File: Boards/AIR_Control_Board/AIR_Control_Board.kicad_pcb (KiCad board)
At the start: 2 copper layers, 65 x 55 mm, 79 parts, among them IC1 ATMEGA16M1, J1 MicroFit_RA_10, J2 MM_F_VT_20, J3 MicroFit_RA_V_2, J4 CONN_02X03, Q1 SSM3K333R, Q2 SSM3K333R, Q3 SSM3K333R, Q4 SSM3K333R, Q5 SSM3K333R, Q6 SSM3K333R, U1 MCP2561-E_SN, U2 TPS561201, Y1 Crystal_SMD

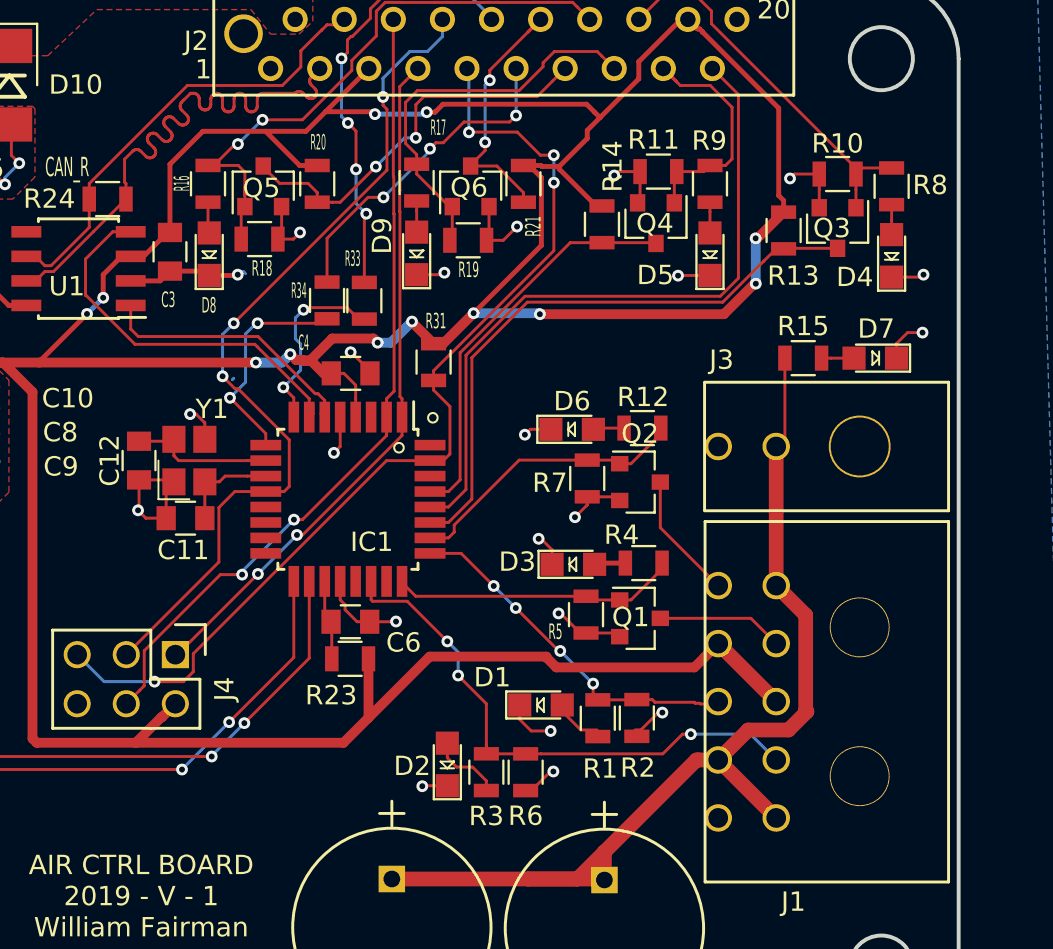
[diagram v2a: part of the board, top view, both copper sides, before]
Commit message: new gbr file with better annotations
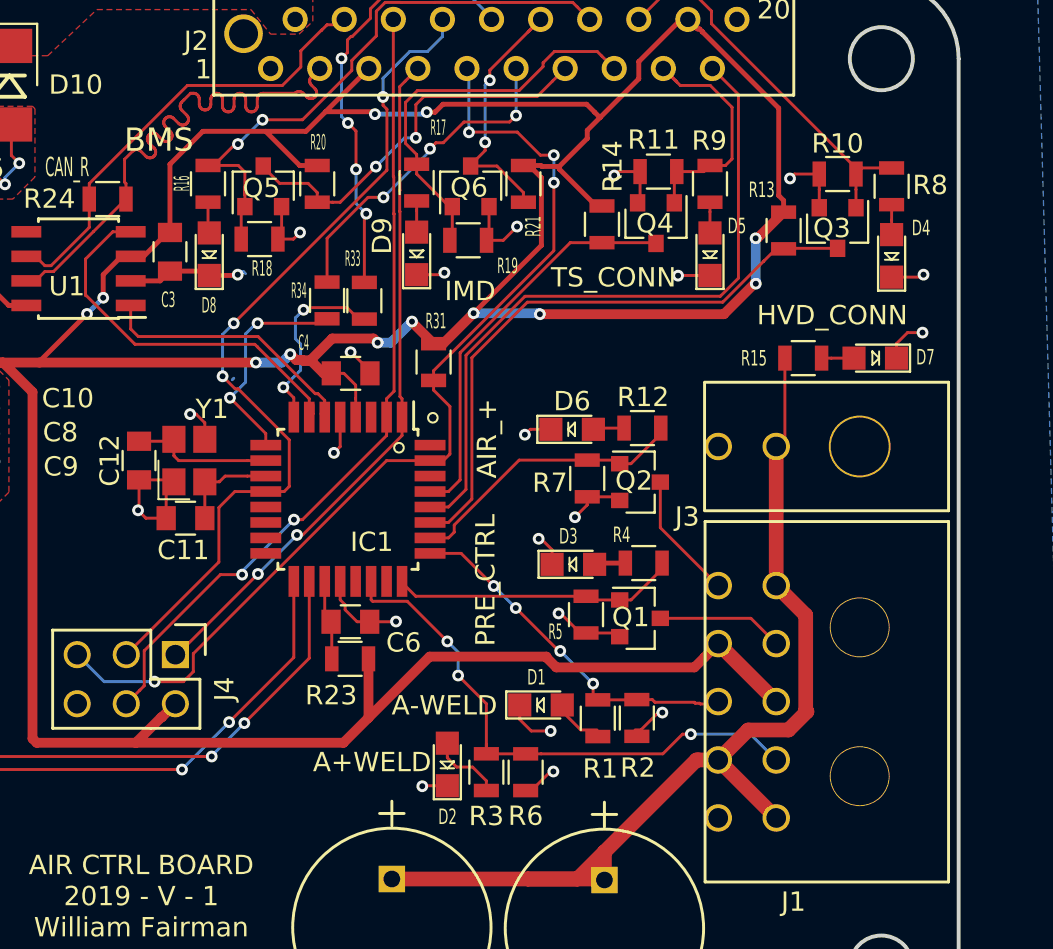
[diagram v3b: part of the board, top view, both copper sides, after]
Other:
- board text added: "A+WELD"
- board text added: "A-WELD"
- board text added: "AIR_+"
- board text added: "BMS"
- board text added: "HVD_CONN"
- board text added: "IMD"
- board text added: "PRE_CTRL"
- board text added: "TS_CONN"
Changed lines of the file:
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@@
   (general
     (thickness 1.6)
-    (drawings 30)
+    (drawings 38)
     (tracks 1023)
     (zones 0)
@@
   )
   (setup
-    (last_trace_width 0.1524)
+    (last_trace_width 0.254)
     (user_trace_width 0.1524)
     (user_trace_width 0.254)
@@
     (tags "LED led 0805 SMD smd SMT smt smdled SMDLED smtled SMTLED")
     (attr smd)
-    (fp_text reference D1 (at -2.51986 -1.42494) (layer F.SilkS)
-      (effects (font (size 1 1) (thickness 0.15)))
+    (fp_text reference D1 (at -0.23894 -1.43002) (layer F.SilkS)
+      (effects (font (size 0.8 0.5) (thickness 0.125)))
     )
     (fp_text value LED_0805 (at 0.508 2.032) (layer F.Fab) hide
@@
     (tags "resistor 0805")
     (attr smd)
-    (fp_text reference R13 (at 2.34188 -0.50292) (layer F.SilkS)
-      (effects (font (size 1 1) (thickness 0.15)))
+    (fp_text reference R13 (at -2.10312 1.13284) (layer F.SilkS)
+      (effects (font (size 0.8 0.5) (thickness 0.125)))
     )
     (fp_text value R_10K (at 0 1.75 270) (layer F.Fab) hide
@@
     (tags "resistor 0805")
     (attr smd)
-    (fp_text reference R15 (at 0 -1.651) (layer F.SilkS)
-      (effects (font (size 1 1) (thickness 0.15)))
+    (fp_text reference R15 (at -2.55016 0.01016) (layer F.SilkS)
+      (effects (font (size 0.8 0.5) (thickness 0.125)))
     )
     (fp_text value R_1K (at 0 1.75) (layer F.Fab) hide
@@
     (tags SOT-23)
     (attr smd)
-    (fp_text reference Q2 (at 0 -2.5) (layer F.SilkS)
+    (fp_text reference Q2 (at -0.31242 -0.06858) (layer F.SilkS)
       (effects (font (size 1 1) (thickness 0.15)))
     )
@@
     (tags "LED led 0805 SMD smd SMT smt smdled SMDLED smtled SMTLED")
     (attr smd)
-    (fp_text reference D3 (at -2.9005 -0.127) (layer F.SilkS)
-      (effects (font (size 1 1) (thickness 0.15)))
+    (fp_text reference D3 (at -0.26144 -1.4478) (layer F.SilkS)
+      (effects (font (size 0.8 0.5) (thickness 0.125)))
     )
     (fp_text value LED_0805 (at 0.508 2.032) (layer F.Fab) hide
@@
     (tags "resistor 0805")
     (attr smd)
-    (fp_text reference R19 (at 0.02286 1.52908) (layer F.SilkS)
+    (fp_text reference R19 (at 2.03962 1.32588) (layer F.SilkS)
       (effects (font (size 0.8 0.4) (thickness 0.1)))
     )
@@
     (tags "LED led 0805 SMD smd SMT smt smdled SMDLED smtled SMTLED")
     (attr smd)
-    (fp_text reference D5 (at -1.0844 -2.82448 180) (layer F.SilkS)
-      (effects (font (size 1 1) (thickness 0.15)))
+    (fp_text reference D5 (at 1.46068 1.39192 180) (layer F.SilkS)
+      (effects (font (size 0.8 0.5) (thickness 0.125)))
     )
     (fp_text value LED_0805 (at 0.508 2.032 90) (layer F.Fab) hide
@@
     (tags "LED led 0805 SMD smd SMT smt smdled SMDLED smtled SMTLED")
     (attr smd)
-    (fp_text reference D4 (at -1.1 -1.905 180) (layer F.SilkS)
-      (effects (font (size 1 1) (thickness 0.15)))
+    (fp_text reference D4 (at 1.44 1.524 180) (layer F.SilkS)
+      (effects (font (size 0.8 0.5) (thickness 0.125)))
     )
     (fp_text value LED_0805 (at 0.508 2.032 90) (layer F.Fab) hide
@@
     (tags "LED led 0805 SMD smd SMT smt smdled SMDLED smtled SMTLED")
     (attr smd)
-    (fp_text reference D2 (at -0.084 -1.8161) (layer F.SilkS)
-      (effects (font (size 1 1) (thickness 0.15)))
+    (fp_text reference D2 (at -2.71036 0.01016) (layer F.SilkS)
+      (effects (font (size 0.8 0.5) (thickness 0.125)))
     )
     (fp_text value LED_0805 (at 0.508 2.032 90) (layer F.Fab) hide
@@
     (attr smd)
     (fp_text reference R4 (at 1.143 1.4605 180) (layer F.SilkS)
-      (effects (font (size 1 1) (thickness 0.15)))
+      (effects (font (size 0.8 0.5) (thickness 0.125)))
     )
     (fp_text value R_200 (at 0 1.75 180) (layer F.Fab) hide
@@
   (module footprints:MicroFit_RA_V_2 (layer F.Cu)
     (at 183.896 106.934 270)
-    (fp_text reference J3 (at -4.48056 7.14756 180) (layer F.SilkS)
+    (fp_text reference J3 (at 3.6322 8.92556 180) (layer F.SilkS)
       (effects (font (size 1 1) (thickness 0.15)))
     )
@@
     (tags "LED led 0805 SMD smd SMT smt smdled SMDLED smtled SMTLED")
     (attr smd)
-    (fp_text reference D7 (at -0.04844 1.51892 180) (layer F.SilkS)
-      (effects (font (size 1 1) (thickness 0.15)))
+    (fp_text reference D7 (at -2.59352 0.04572 180) (layer F.SilkS)
+      (effects (font (size 0.8 0.5) (thickness 0.125)))
     )
     (fp_text value LED_0805 (at 0.508 2.032 180) (layer F.Fab) hide
@@
       (xy 21.61435 26.216765) (xy 21.849605 26.21762) (xy 22.074352 26.216386)) (layer B.SilkS) (width 0.01))
   )
+  (gr_text A-WELD (at 162.41268 120.33504) (layer F.SilkS)
+    (effects (font (size 1 1) (thickness 0.15)))
+  )
+  (gr_text A+WELD (at 158.66872 123.27128) (layer F.SilkS)
+    (effects (font (size 1 1) (thickness 0.15)))
+  )
+  (gr_text BMS (at 147.63496 91.07424) (layer F.SilkS)
+    (effects (font (size 1.2 1.2) (thickness 0.18)))
+  )
+  (gr_text IMD (at 163.73856 98.89744) (layer F.SilkS)
+    (effects (font (size 1 1) (thickness 0.2)))
+  )
+  (gr_text TS_CONN (at 171.16044 98.19132) (layer F.SilkS)
+    (effects (font (size 1 1) (thickness 0.15)))
+  )
+  (gr_text HVD_CONN (at 182.4736 100.14712) (layer F.SilkS)
+    (effects (font (size 1 1) (thickness 0.15)))
+  )
+  (gr_text AIR_+ (at 164.6174 106.52252 90) (layer F.SilkS)
+    (effects (font (size 1 1) (thickness 0.15)))
+  )
+  (gr_text PRE_CTRL (at 164.53612 113.84788 90) (layer F.SilkS)
+    (effects (font (size 1 1) (thickness 0.15)))
+  )
   (gr_text "AIR CTRL BOARD\n2019 - V - 1\nWilliam Fairman" (at 146.72564 130.20548) (layer F.SilkS)

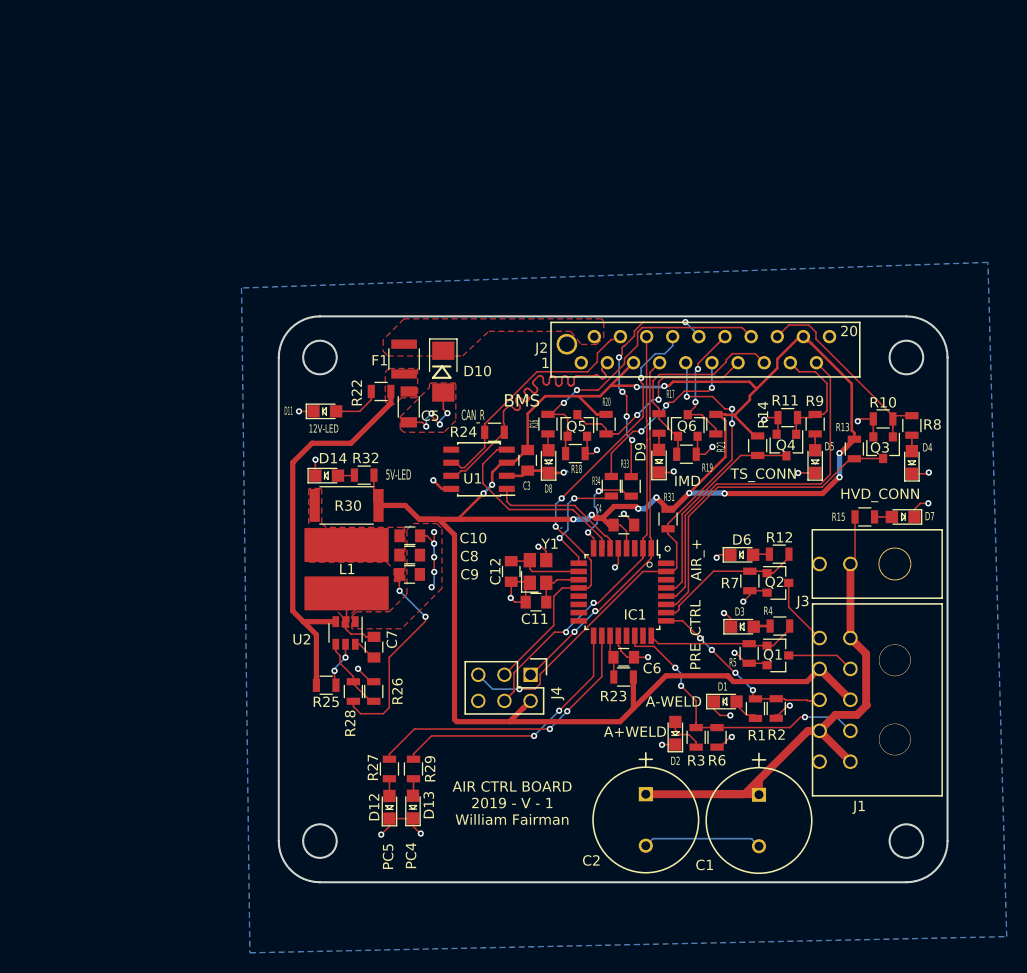
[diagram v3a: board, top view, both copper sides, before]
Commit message: updated air ctrl board and sensing board
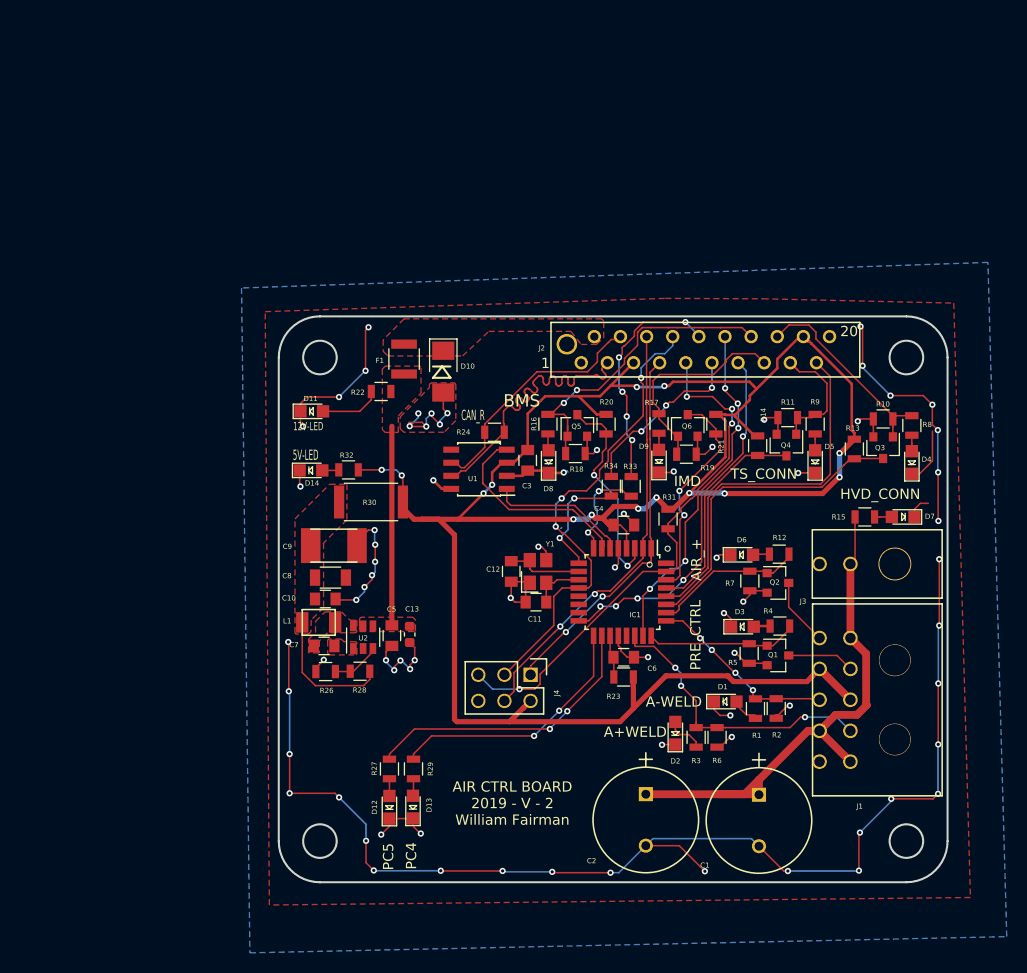
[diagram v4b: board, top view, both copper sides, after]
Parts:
- removed R25: R_10K, footprints:R_0805_OEM
- added C13: C_2.2uF, footprints:C_0603_1608Metric, F.Cu at (136.7, 113.8)
- C10: value C_0.1uF -> C_47uF
- C5: value C_22uF -> C_0.1uF; footprint footprints:C_1206_OEM -> footprints:C_0805_OEM
- C8: value C_47uF -> C_22uF; footprint footprints:C_0805_OEM -> footprints:C_1206_OEM
- C9: value C_1uF -> C_33uF; footprint footprints:C_0805_OEM -> footprints:C_1812_updated
- L1: value L_4.7uH -> L_100uH; footprint footprints:4.7uH_Inductor_OEM -> footprints:L_100uH
- R26: value R_10K -> R_25K
- R28: value R_51.1K -> R_100K
- U2: value TPS561201 -> TPS560430YF
- moved C5 22.3 mm to (135.0, 113.9)
- moved C10 10.3 mm to (128.5, 110.3)
- moved C9 10.0 mm to (127.1, 105.2)
- moved C8 8.00 mm to (129.0, 108.3)
- moved L1 5.84 mm to (127.9, 112.6), turned to 180 degrees
- moved R26 5.06 mm to (128.6, 117.4), turned to 180 degrees
- moved C7 4.85 mm to (128.4, 114.9), turned to 180 degrees
- moved R30 2.40 mm to (133.0, 100.9)
- moved R28 2.07 mm to (131.9, 117.4), turned to 180 degrees
- moved U2 1.76 mm to (132.2, 114.1), turned to 90 degrees
- moved D14 1.61 mm to (127.1, 97.8)
- moved R32 1.61 mm to (130.8, 97.8)
- moved D11 1.27 mm to (127.2, 92.1)
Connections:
- C5 pad 1: /12V_Fused -> Net-(C13-Pad1)
- F1 pad 2: /12V_Fused -> Net-(C13-Pad1)
- IC1 pad 16: Net-(IC1-Pad16) -> /BMS_Sense
- IC1 pad 23: Net-(IC1-Pad23) -> /IMD_Sense
- IC1 pad 3: Net-(IC1-Pad3) -> /ss_BMS
- IC1 pad 30: Net-(IC1-Pad30) -> /ss_IMD
- Q5 pad 3: /BMS_Sense -> /ss_BMS
- Q6 pad 3: /IMD_Sense -> /ss_IMD
- R20 pad 2: /BMS_Sense -> /ss_BMS
- R21 pad 2: /IMD_Sense -> /ss_IMD
- R22 pad 1: /12V_Fused -> Net-(C13-Pad1)
- U2 pad 1: GND -> Net-(C7-Pad1)
- U2 pad 2: Net-(C7-Pad2) -> GND
- U2 pad 3: /12V_Fused -> Net-(R26-Pad1)
- U2 pad 4: Net-(R26-Pad1) -> Net-(C13-Pad1)
- U2 pad 5: Net-(R25-Pad1) -> Net-(C13-Pad1)
- U2 pad 6: Net-(C7-Pad1) -> Net-(C7-Pad2)
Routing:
- net GND: track 101.9 -> 267.3 mm, vias 37 -> 74
- net /12V_Fused: track 38.8 -> 0.00 mm
- net /ss_IMD: track 0.00 -> 21.3 mm, vias 0 -> 2
- net /ss_BMS: track 0.00 -> 20.5 mm, vias 0 -> 2
- net /IMD_Sense: track 13.8 -> 33.9 mm, vias 2 -> 5
- net Net-(C13-Pad1): track 0.00 -> 19.3 mm
- net /BMS_Sense: track 20.6 -> 36.0 mm, vias 2 -> 5
- net Net-(C10-Pad1): track 20.0 -> 13.0 mm, vias 2 -> 0
- net Net-(C7-Pad2): track 6.57 -> 0.00 mm
- net Net-(R25-Pad1): track 4.48 -> 0.00 mm, vias 2 -> 0
- net Net-(R26-Pad1): track 7.25 -> 4.76 mm
- net Net-(C7-Pad1): track 2.35 -> 0.00 mm
- net VCC: track 212.6 -> 214.7 mm, vias 12 -> 14
- net /MISO: track 35.9 -> 37.6 mm
- net Net-(D11-Pad2): track 4.69 -> 5.96 mm
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- added copper zone on F.Cu, net Net-(C13-Pad1)
- added copper zone on F.Cu, net Net-(C7-Pad1)
- removed copper zone on F.Cu, net /12V_Fused
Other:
- board text added: "AIR CTRL BOARD 2019 - V - 2 William Fairman"
- board text removed: "AIR CTRL BOARD 2019 - V - 1 William Fairman"
